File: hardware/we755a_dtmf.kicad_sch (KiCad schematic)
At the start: 44 parts, among them J1 Conn_01x06_Male, J2 UPDI, J3 Conn_02x10_Odd_Even, U1 AVR128DA28-I/SS, U2 MT8870, U3 H11AA1, U4 LAA108, U5 LAA108, U6 LAA108, U7 LAA108, U8 LAA108, Y1 32.767KHz, Y2 3.579545MHZ

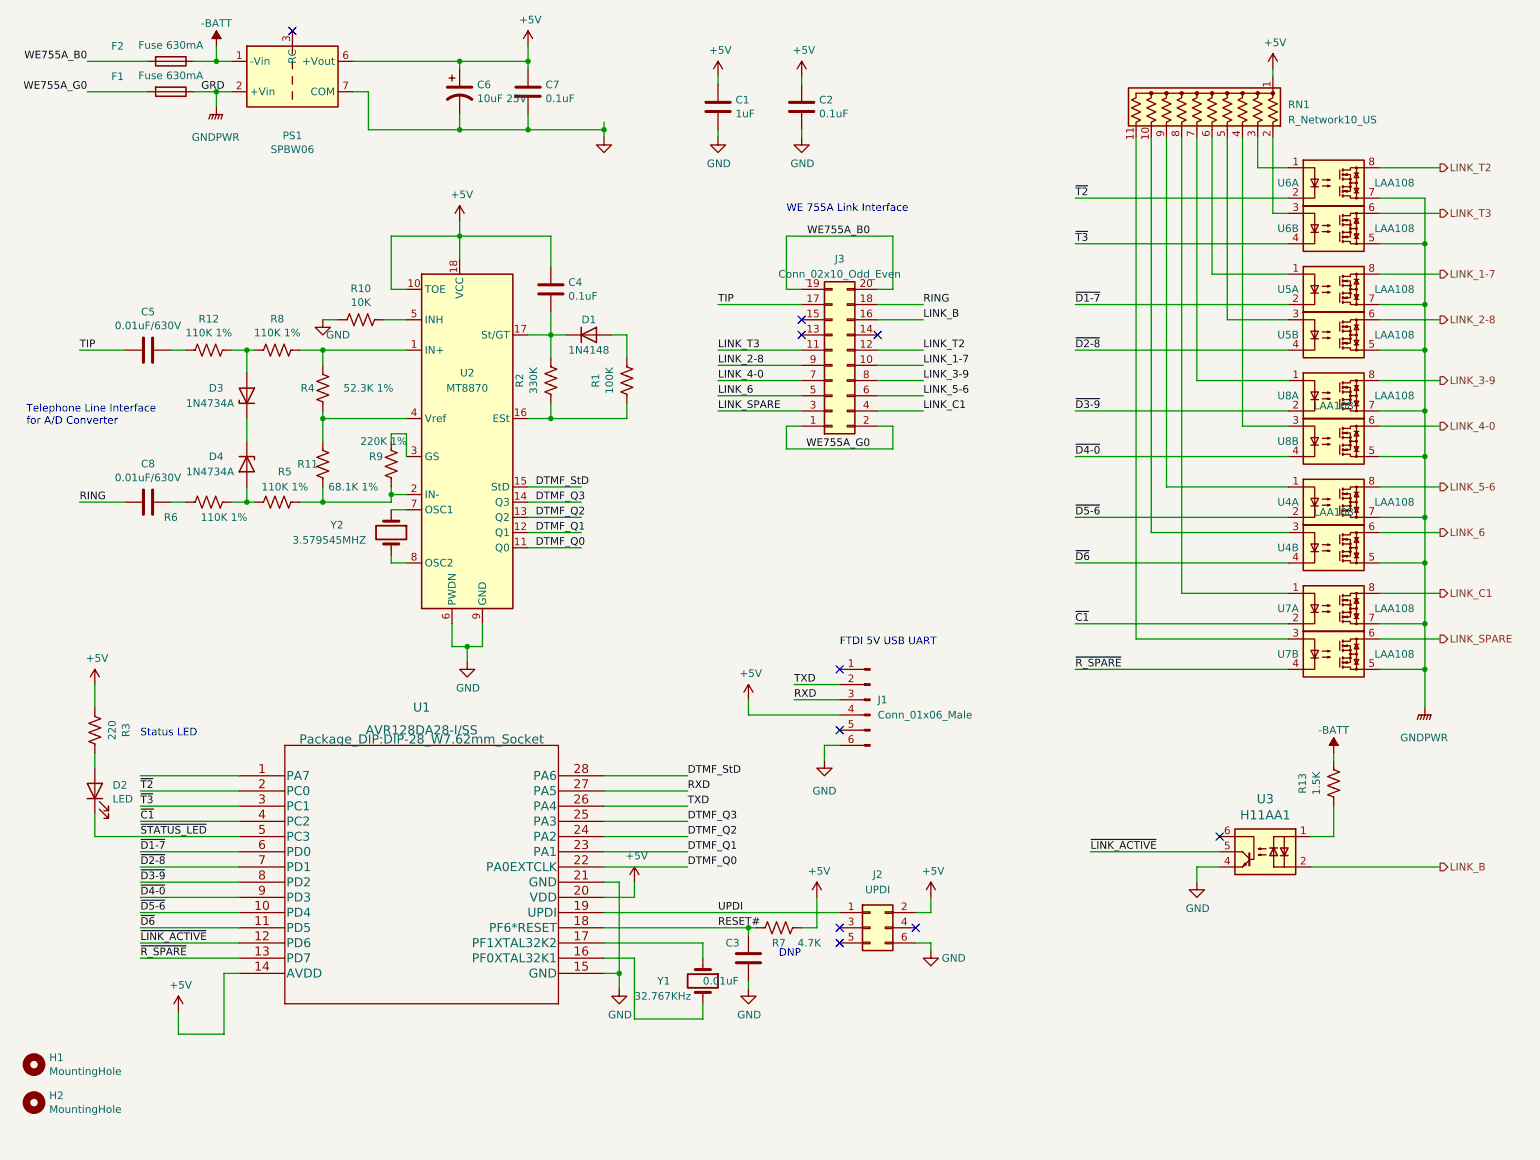
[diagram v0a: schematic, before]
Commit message: Update PCB to Rev2: No functional changes.
    * Rev 1 and Rev 2 PCBs are identical except for the silkscreen.
    * Rename LINK_B to LINK_E on schematic and layout.
    * Correct value of C1 on schematic.
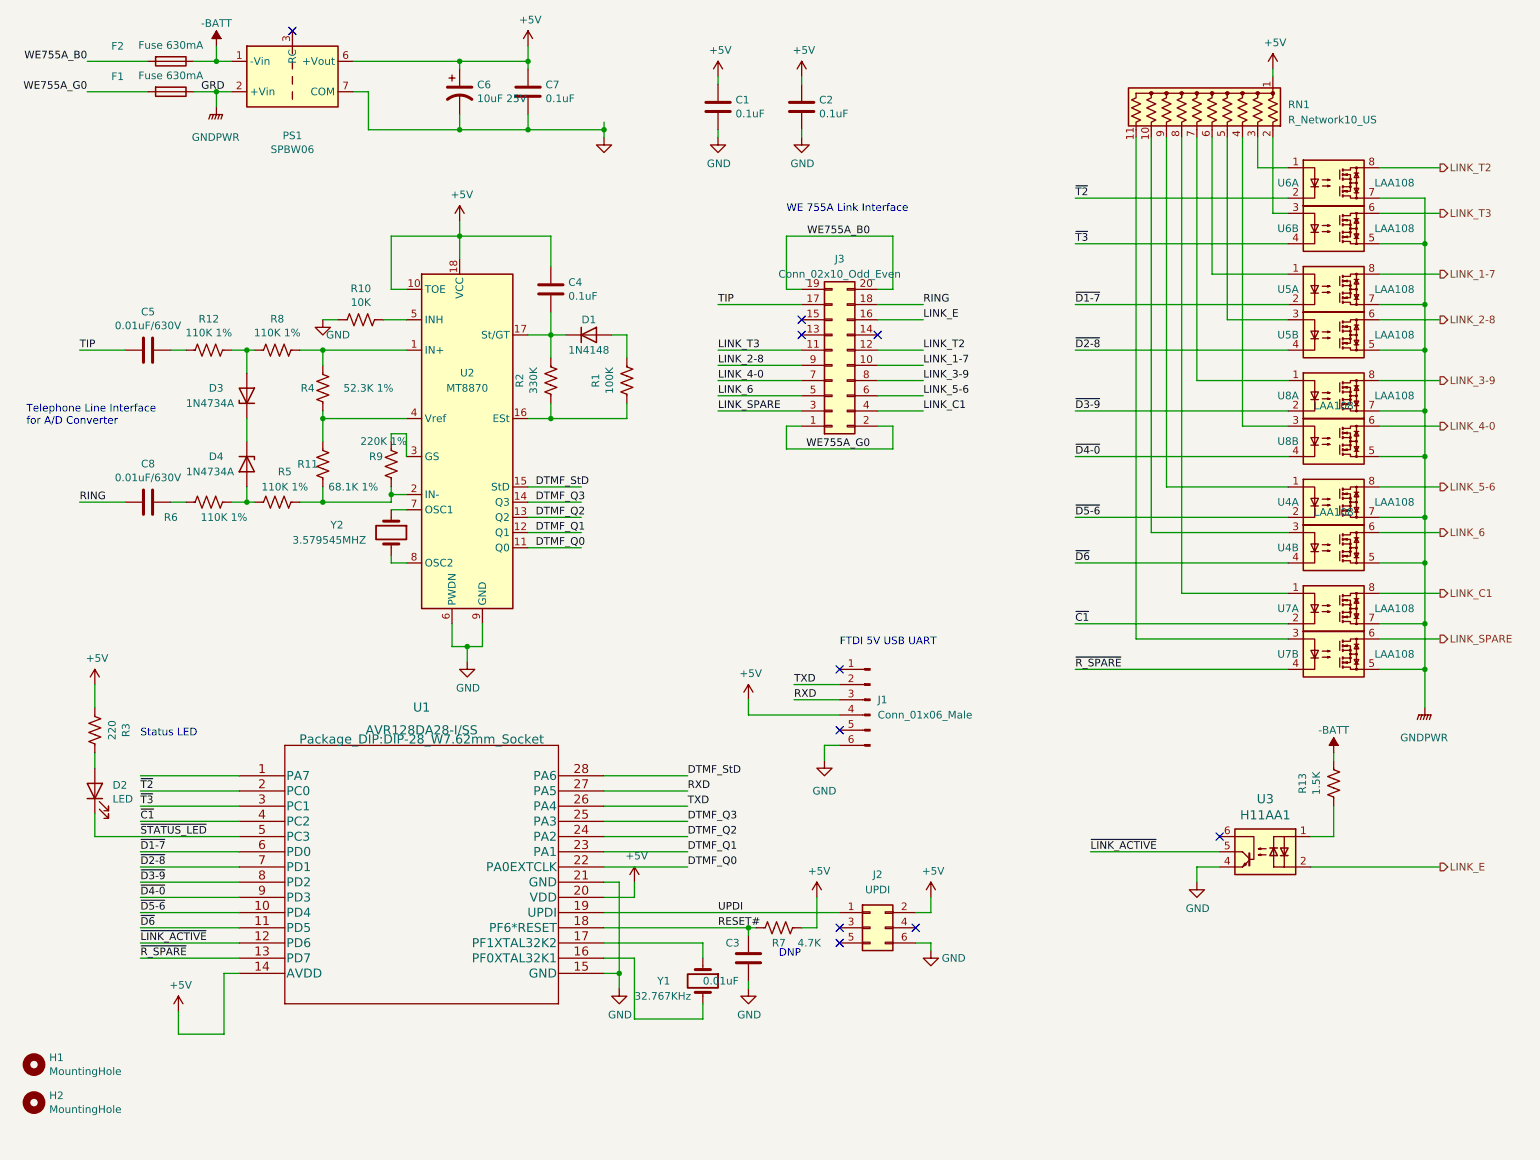
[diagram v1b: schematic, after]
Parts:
- C1: value 1uF -> 0.1uF
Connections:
- net LINK_B renamed LINK_E
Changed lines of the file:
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@@
   (title_block
     (title "WE 755A PBX DTMF Converter")
-    (date "2023-06-03")
-    (rev "1")
+    (date "2023-07-04")
+    (rev "2")
     (company "Howard M. Harte")
     (comment 1 "https://github.com/hharte/we755a_dtmf")
@@
     (effects (font (size 1.27 1.27)) (justify right bottom))
   )
-  (label "LINK_B" (at 167.64 63.5 0) (fields_autoplaced)
+  (label "LINK_E" (at 167.64 63.5 0) (fields_autoplaced)
     (effects (font (size 1.27 1.27)) (justify left bottom))
   )
@@
     (effects (font (size 1.27 1.27)) (justify left))
   )
-  (hierarchical_label "LINK_B" (shape output) (at 254 154.94 0) (fields_autoplaced)
+  (hierarchical_label "LINK_E" (shape output) (at 254 154.94 0) (fields_autoplaced)
     (effects (font (size 1.27 1.27)) (justify left))
   )
@@
       (effects (font (size 1.27 1.27)) (justify left))
     )
-    (property "Value" "1uF" (at 136.271 29.083 0)
+    (property "Value" "0.1uF" (at 136.271 29.083 0)
       (effects (font (size 1.27 1.27)) (justify left))
     )

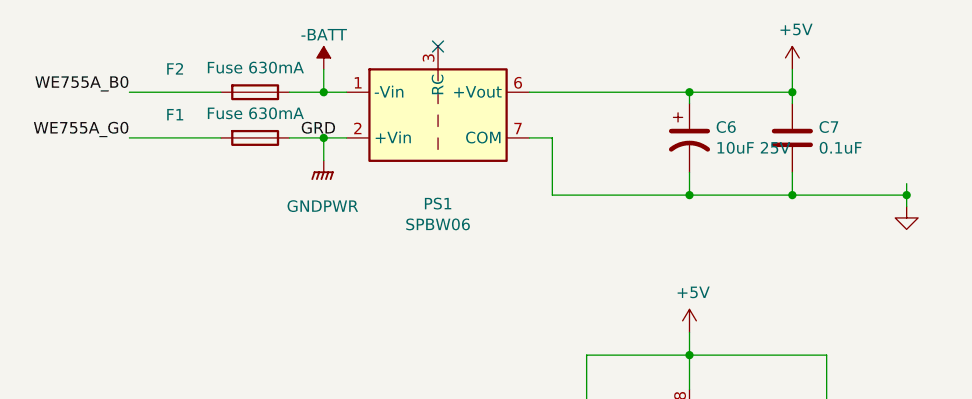
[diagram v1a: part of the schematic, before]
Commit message: Update to KiCAD 8.0.1.
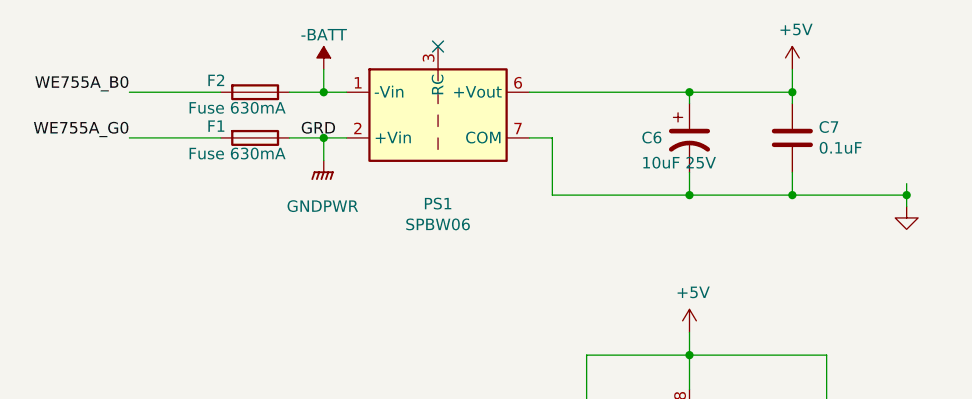
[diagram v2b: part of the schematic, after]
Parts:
- C1, C2, C4: Digi-Key_PN (none) -> 56-K104M15X7RF5TL2CT-ND; MPN (none) -> K104M15X7RF5TL2
- C5, C8: Digi-Key_PN (none) -> 490-8927-ND; MPN (none) -> RDER72J103K2K1H03B
- C7: Digi-Key_PN  (none) -> 56-K104M15X7RF5TL2CT-ND; MPN (none) -> K104M15X7RF5TL2
- D3, D4: Digi-Key_PN (none) -> 1N4734A-T50ACT-ND; MPN (none) -> 1N4734A-T50A
- H1, H2: now left out of the parts list
- R12, R5, R6, R8: Digi-Key_PN (none) -> 110KXBK-ND; MPN (none) -> MFR-25FBF52-110K
